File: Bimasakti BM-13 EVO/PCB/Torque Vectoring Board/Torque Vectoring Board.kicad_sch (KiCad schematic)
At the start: 1 part

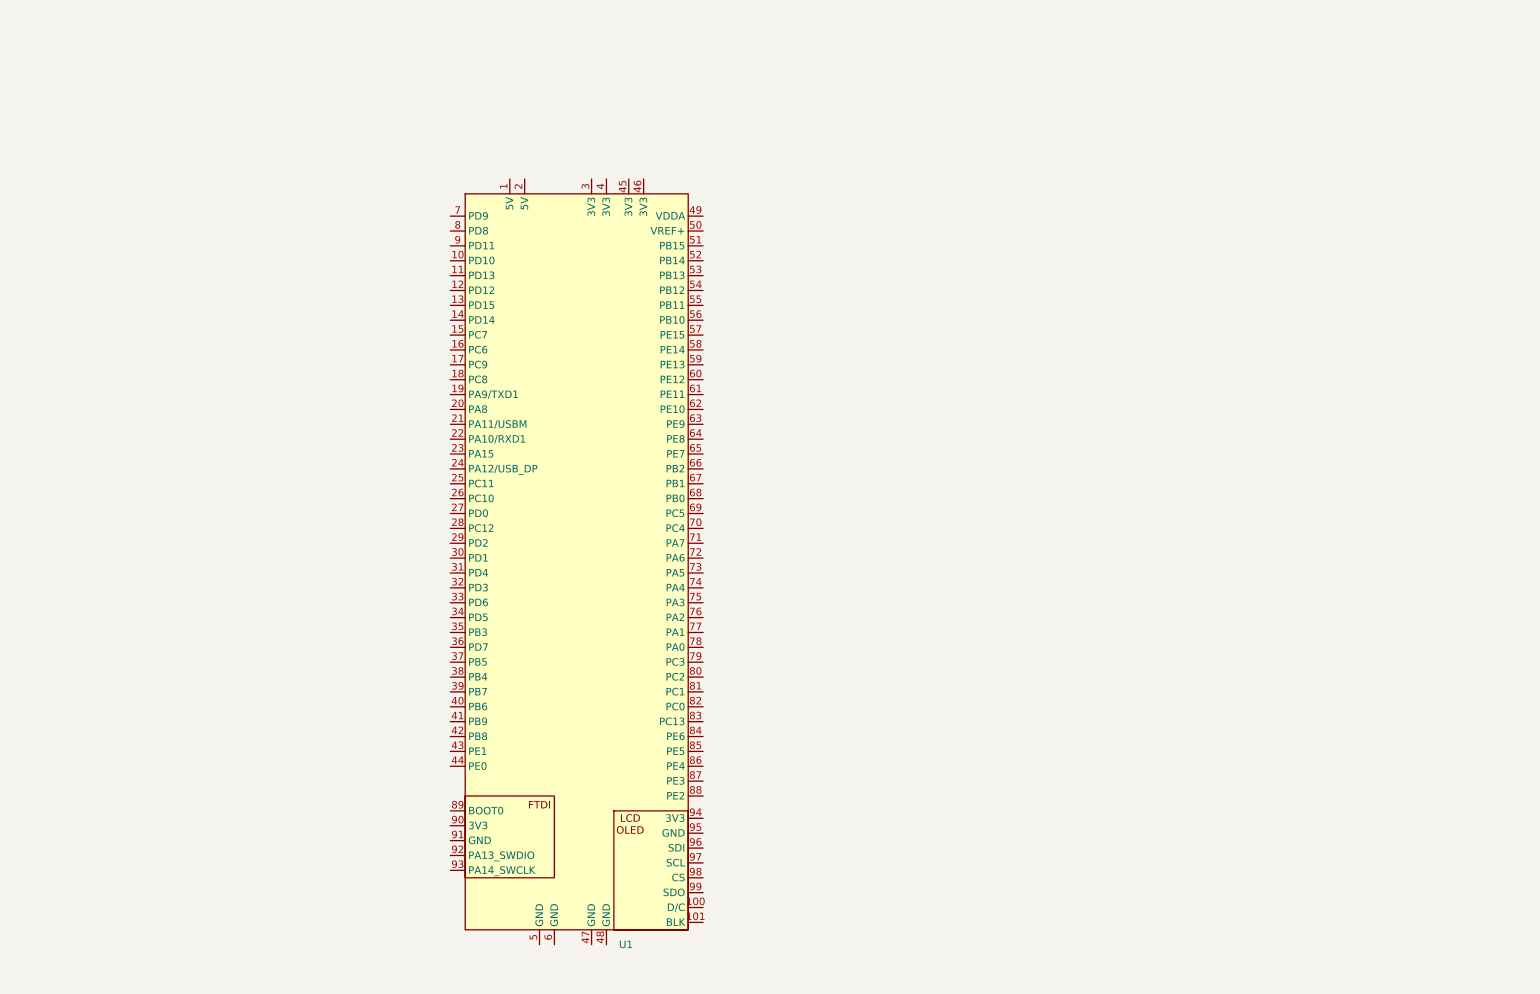
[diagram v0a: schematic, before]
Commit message: torque vectoring
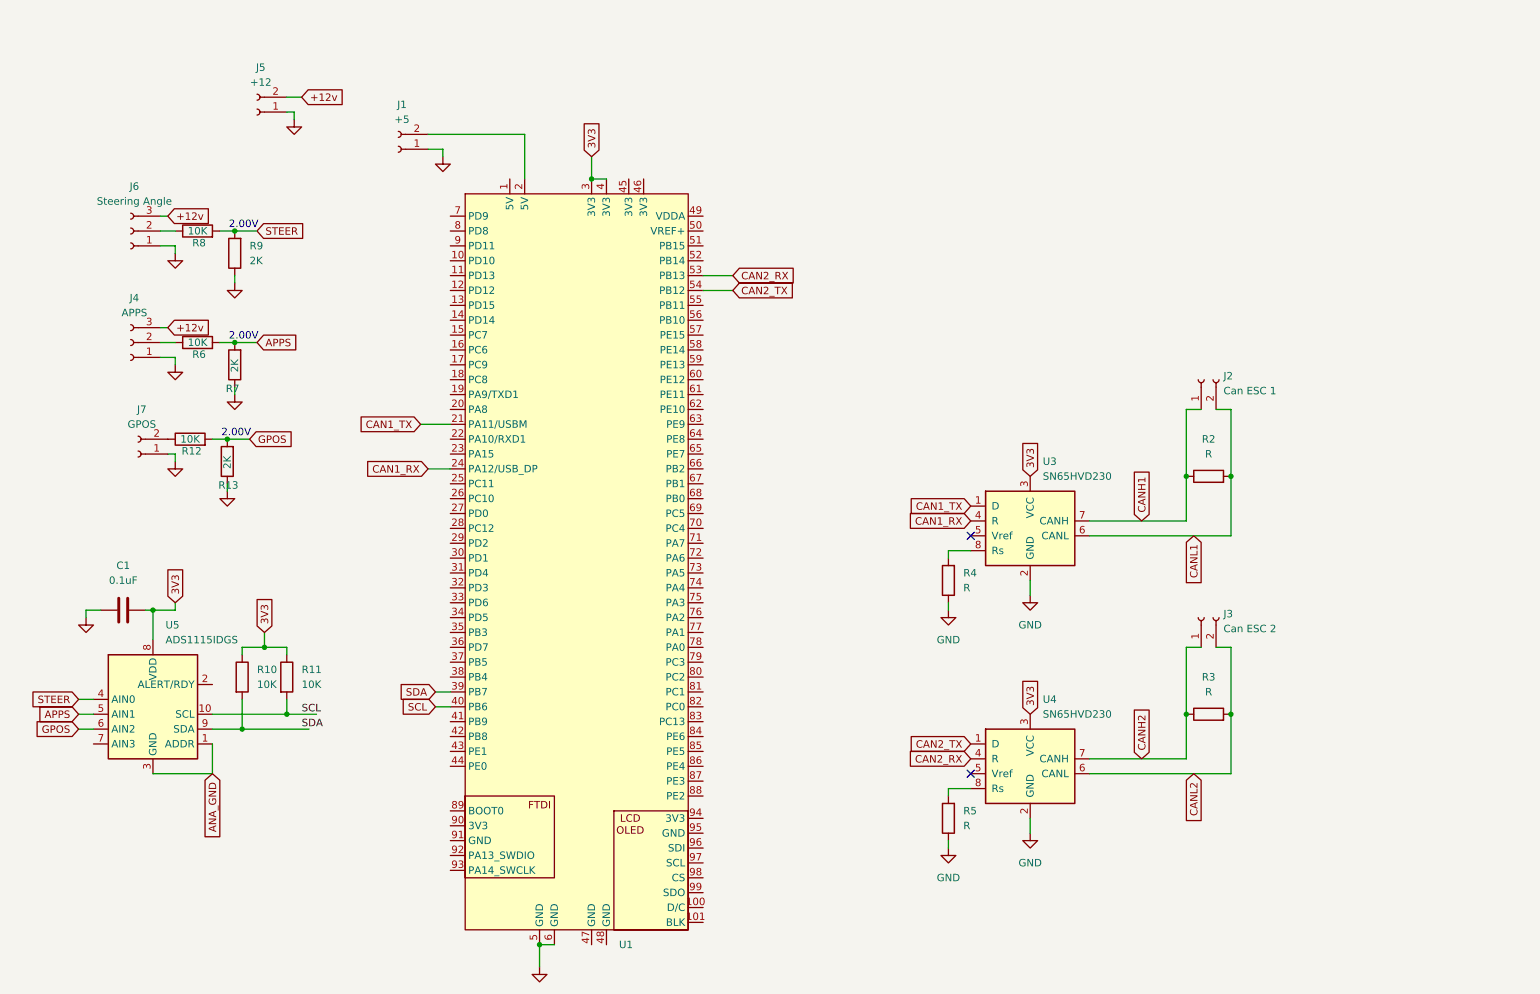
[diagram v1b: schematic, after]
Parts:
- added C1: 0.1uF, Capacitor_SMD:C_0603_1608Metric, symbol Device:C
- added J1: +5, Connector_JST:JST_EH_B2B-EH-A_1x02_P2.50mm_Vertical, symbol Connector:Conn_01x02_Socket
- added J2: Can ESC 1, Connector_JST:JST_EH_B2B-EH-A_1x02_P2.50mm_Vertical, symbol Connector:Conn_01x02_Socket
- added J3: Can ESC 2, Connector_JST:JST_EH_B2B-EH-A_1x02_P2.50mm_Vertical, symbol Connector:Conn_01x02_Socket
- added J4: APPS, symbol Connector:Conn_01x03_Socket
- added J5: +12, Connector_JST:JST_EH_B2B-EH-A_1x02_P2.50mm_Vertical, symbol Connector:Conn_01x02_Socket
- added J6: Steering Angle, symbol Connector:Conn_01x03_Socket
- added J7: GPOS, symbol Connector:Conn_01x02_Socket
- added R10, R11, R12, R6, R8: 10K, Resistor_SMD:R_0805_2012Metric, symbol Device:R
- added R13, R7, R9: 2K, Resistor_SMD:R_0805_2012Metric, symbol Device:R
- added R2, R3, R4, R5: R, Resistor_SMD:R_0805_2012Metric, symbol Device:R
- added U3, U4: SN65HVD230, Package_SO:SOIC-8_3.9x4.9mm_P1.27mm, symbol Interface_CAN_LIN:SN65HVD230
- added U5: ADS1115IDGS, Package_SO:TSSOP-10_3x3mm_P0.5mm, symbol Analog_ADC:ADS1115IDGS
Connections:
- net at U1.2 (5V): now also J1.2 (Pin_2)
- net CAN1_TX: now reaches U1.21 (PA11/USBM)
- net CAN1_TX: now also U3.1 (D)
- net CAN1_RX: now reaches U1.24 (PA12/USB_DP)
- net CAN1_RX: now also U3.4 (R)
- net 3V3: now reaches U1.3 (3V3)
- net 3V3: now also U1.4 (3V3), C1.2, R10.1, R11.1, U3.3 (VCC), U4.3 (VCC), U5.8 (VDD)
- net SDA: now reaches U1.39 (PB7)
- net SDA: now also R10.2, U5.9 (SDA)
- net SCL: now reaches U1.40 (PB6)
- net SCL: now also R11.2, U5.10 (SCL)
- net GND: now reaches U1.5 (GND)
- net GND: now also U1.6 (GND), C1.1, J1.1 (Pin_1), J4.1 (Pin_1), J5.1 (Pin_1), J6.1 (Pin_1), J7.1 (Pin_1), R13.1, R4.1, R5.1, R7.1, R9.1, U3.2 (GND), U4.2 (GND)
- net CAN2_RX: now reaches U1.53 (PB13)
- net CAN2_RX: now also U4.4 (R)
- net CAN2_TX: now reaches U1.54 (PB12)
- net CAN2_TX: now also U4.1 (D)
- new net: J6.2 (Pin_2), R8.1
- new net: R4.2, U3.8 (Rs)
- new net: J4.2 (Pin_2), R6.1
- new net: J7.2 (Pin_2), R12.1
- new net: R5.2, U4.8 (Rs)
- new net +12v: J4.3 (Pin_3), J5.2 (Pin_2), J6.3 (Pin_3)
- new net ANA_GND: U5.1 (ADDR), U5.3 (GND)
- new net APPS: R6.2, R7.2, U5.5 (AIN1)
- new net CANH1: J2.1 (Pin_1), R2.1, U3.7 (CANH)
- new net CANH2: J3.1 (Pin_1), R3.1, U4.7 (CANH)
- new net CANL1: J2.2 (Pin_2), R2.2, U3.6 (CANL)
- new net CANL2: J3.2 (Pin_2), R3.2, U4.6 (CANL)
- new net GPOS: R12.2, R13.2, U5.6 (AIN2)
- new net STEER: R8.2, R9.2, U5.4 (AIN0)
- no-connect marks 0 -> 2
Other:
- note added: "2.00V"

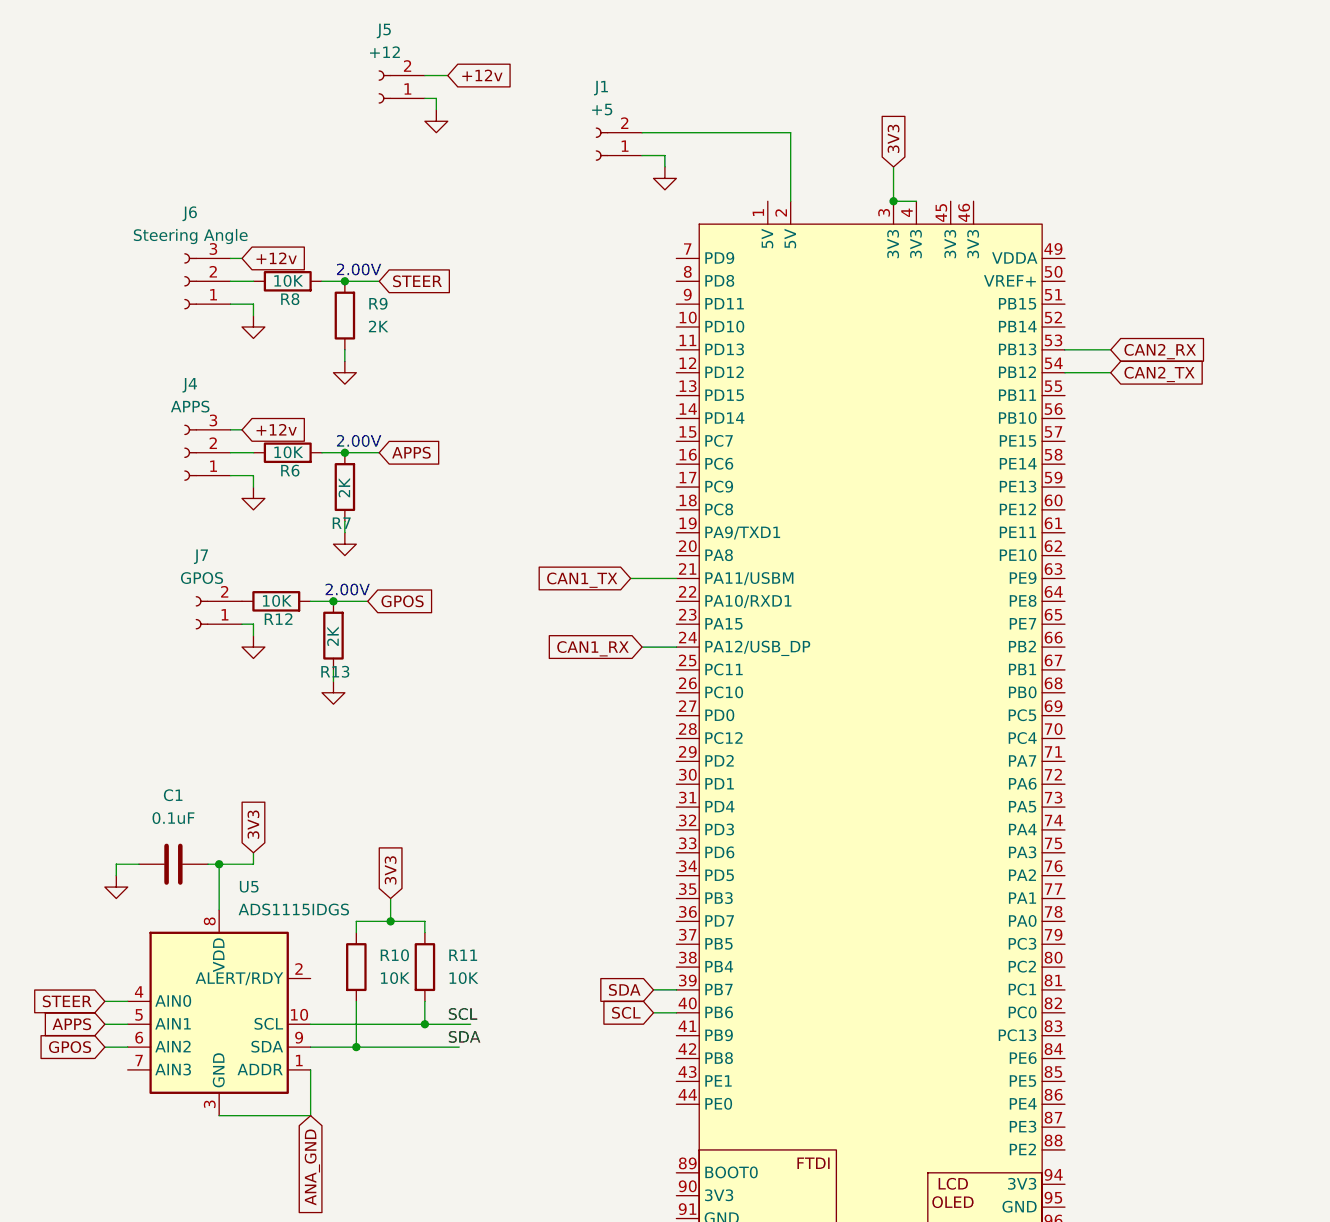
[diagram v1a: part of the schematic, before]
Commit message: update TV board
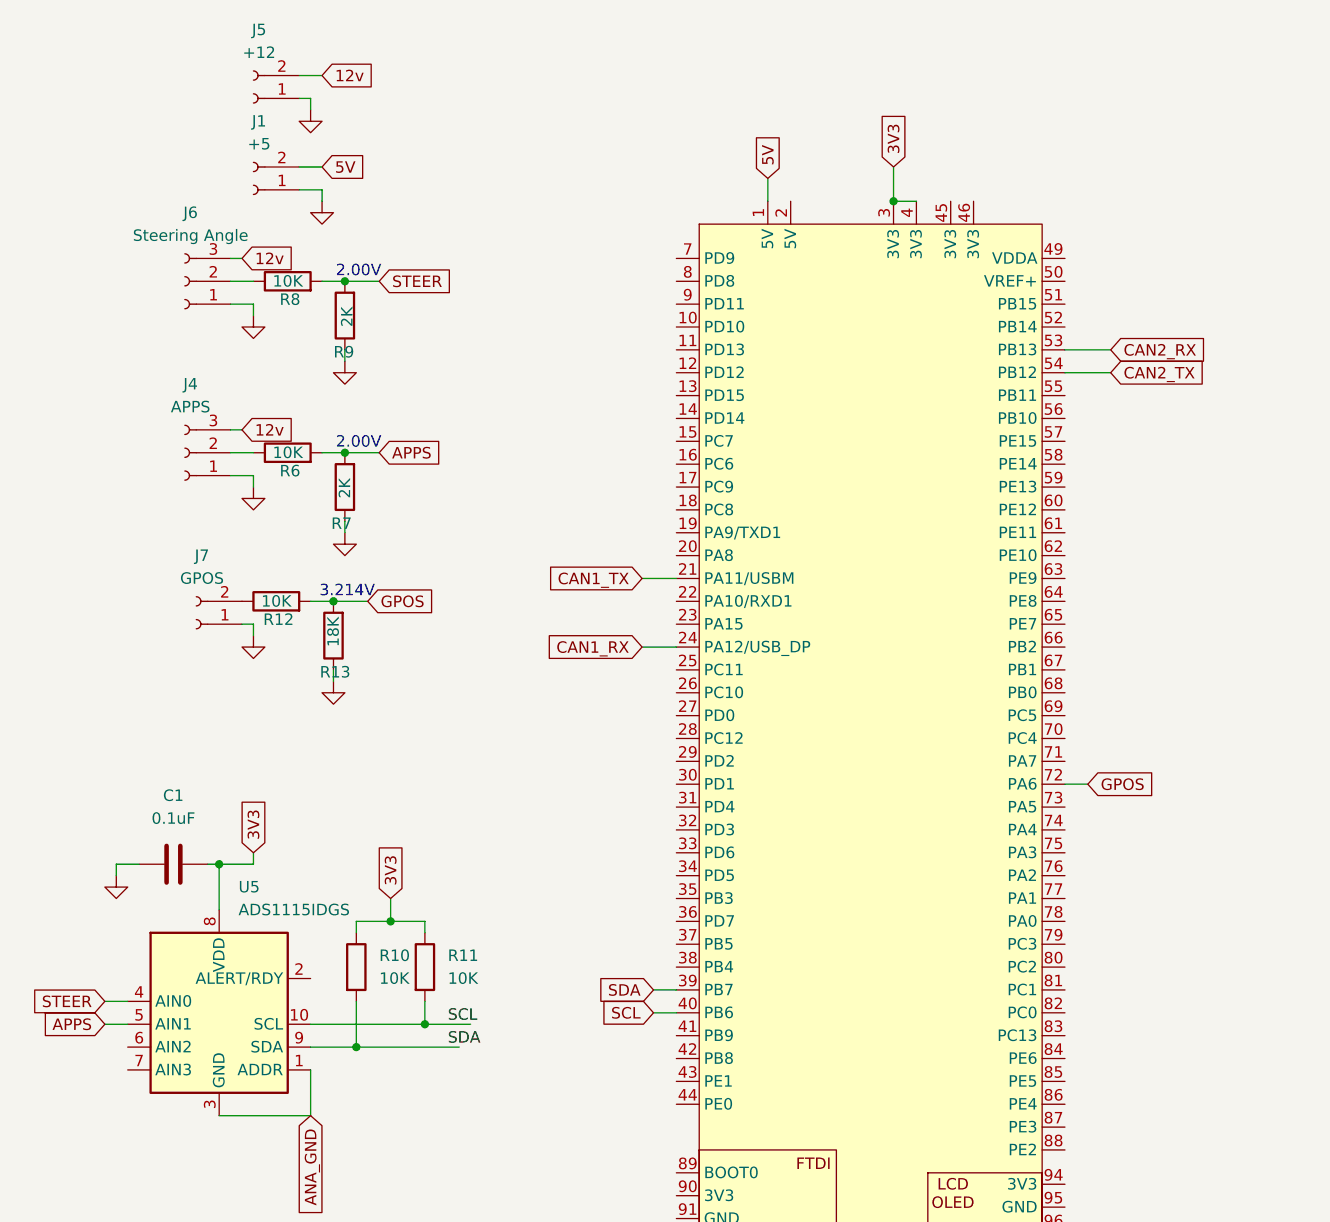
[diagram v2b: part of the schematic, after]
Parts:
- R13: value 2K -> 18K
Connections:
- net GPOS: now also U1.72 (PA6); no longer U5.6 (AIN2)
- net at U1.2 (5V): no longer J1.2 (Pin_2)
- net 5V: now reaches U1.1 (5V)
- net 5V: now also J1.2 (Pin_2)
- net +12v renamed 12v
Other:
- note added: "3.214V"
- moved on the sheet: J1, J5
